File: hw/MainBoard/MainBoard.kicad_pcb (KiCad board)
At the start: 2 copper layers, 150 x 53.5 mm, 208 parts, among them J1 Conn_01x14, J2 Conn_01x03_Female, J3 Conn_01x06_Female, J4 Conn_01x06_Female, K1 EC2-5NU, K2 EC2-5NU, Q1 MMBT3904, Q2 MMBT3904, U1 DPBW03F, U10 OPA2140, U11 TL072, U12 CPC1018N, U13 DG444, U14 DG444, U15 AQY22, U16 AQY22, U17 OPA2140, U18 TL071, U19 OPA140, U2 LT1117-5.0, U20 OPA140, U21 TLP170D, U22 OPA2140, U23 TLC227x, U24 AD7190BRUZ, U25 Si8642BB-B-IS1, U26 ISO1541, U27 MCP23017_SO, U28 24LC01, U3 DG444, U4 OPA2140, U5 OPA2140, U6 OPA2140, U7 LM393, U8 ADR431ARZ, U9 AD5686RBRUZ

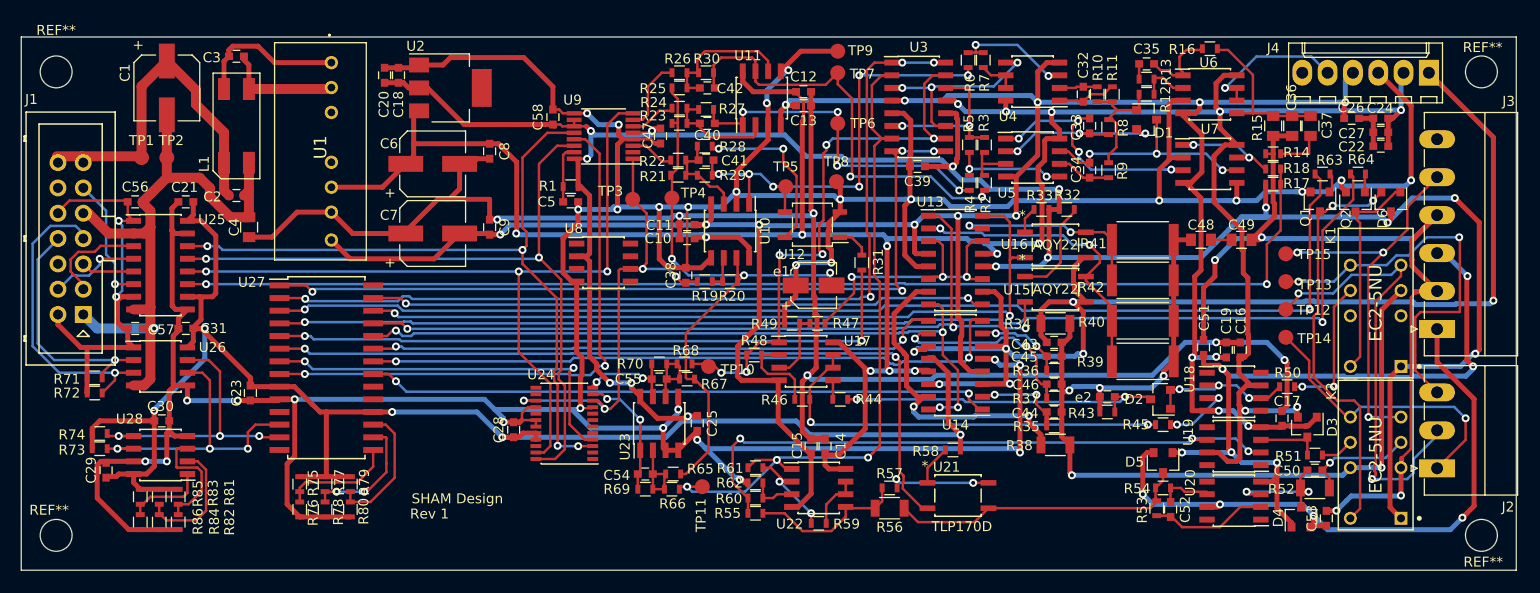
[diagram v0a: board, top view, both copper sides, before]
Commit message: Updated layout with updated schema
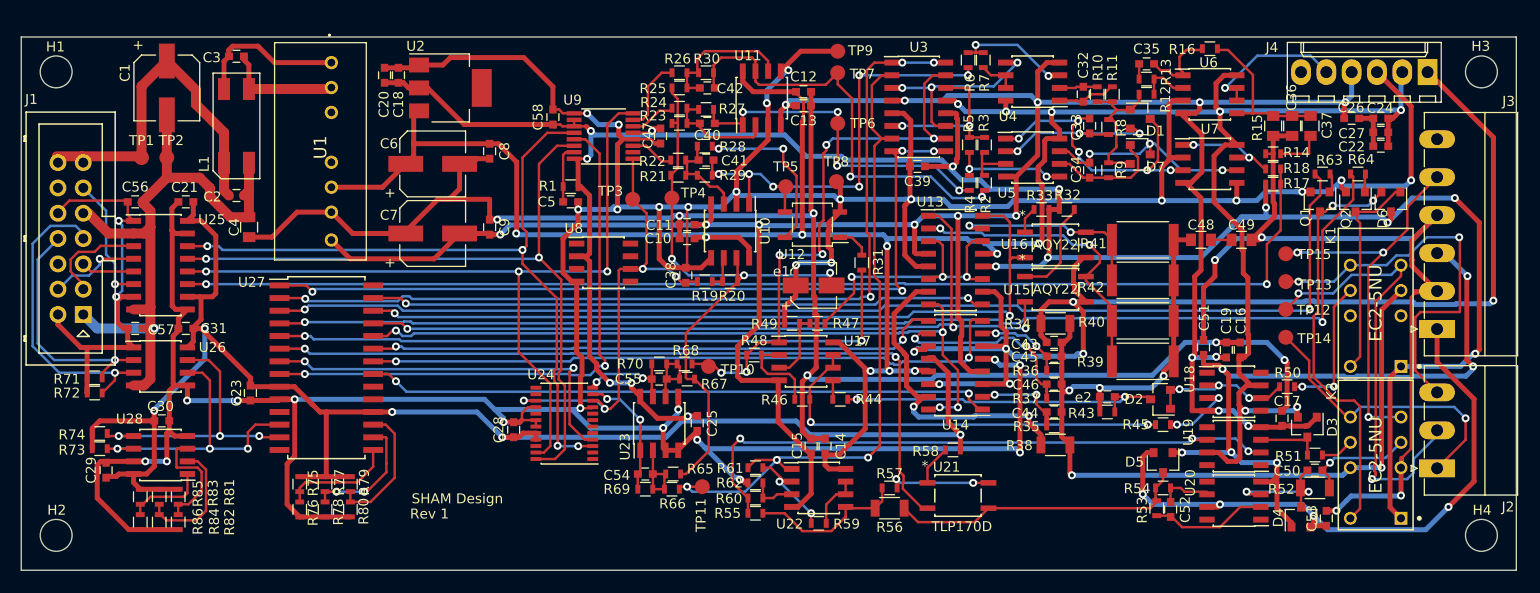
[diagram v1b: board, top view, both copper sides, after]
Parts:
- removed REF** (x4): MountingHole_3.2mm_M3, Mounting_Holes:MountingHole_3.2mm_M3
- added D7: BAV199LT1, TO_SOT_Packages_SMD:SOT-23, F.Cu at (175.8, 61.3)
- added H1: MountingHole, Mounting_Holes:MountingHole_3.2mm_M3, F.Cu at (67.0, 53.0)
- added H2: MountingHole, Mounting_Holes:MountingHole_3.2mm_M3, F.Cu at (67.0, 99.5)
- added H3: MountingHole, Mounting_Holes:MountingHole_3.2mm_M3, F.Cu at (210.0, 53.0)
- added H4: MountingHole, Mounting_Holes:MountingHole_3.2mm_M3, F.Cu at (210.0, 99.5)
- D1: value BAV99S -> BAV99LT1
- moved D1 0.64 mm to (175.8, 57.7)
- moved J4 0.14 mm to (204.6, 53.0)
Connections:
- D1 pad 3: Net-(C34-Pad1) -> Net-(C33-Pad1)
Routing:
- net Net-(C34-Pad2): track 5.49 -> 11.7 mm
- net Net-(C33-Pad1): track 24.4 -> 30.4 mm, vias 4 -> 5
- net Net-(D1-Pad1): track 12.8 -> 14.7 mm
- net /frontend/+15VOUT: track 64.6 -> 63.2 mm
- net Net-(C34-Pad1): track 23.3 -> 21.8 mm
- net Net-(C33-Pad2): track 18.8 -> 18.3 mm
